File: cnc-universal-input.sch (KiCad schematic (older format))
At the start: 125 parts, among them J1 3PT, J10 2PT, J11 8PT, J12 USB_B_Mini, J13 2PT, J14 2PT, J2 3PT, J3 3PT, J4 3PT, J5 3PT, J6 3PT, J7 3PT, J8 3PT, J9 AVR-ISP-6, Q1 2N7002, Q11 2N7002, Q12 2N7002, Q13 2N7002, SW1 RESET, SW2 BTN, U1 ATmega328PB, U10 SFH617A-4, U11 SFH617A-4, U12 SFH617A-4, U13 SFH617A-4, U14 SFH617A-4, U15 SFH617A-4, U16 SFH617A-4, U18 CH340G, U19 TS2596S, U2 74HC595, U3 74HC595, U4 74HC595, U5 4051, U6 TS2596S, U8 LM7321, U9 SFH617A-4, Y1 18.432Mhz, Y2 12MHz

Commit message: Couldn't find a single 328PB non AU
Atmega328PB-AU is the only 328 I could get...
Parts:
- removed R1: 330, Resistor_SMD:R_0805_2012Metric, symbol Device:R_Small
- removed U1: ATmega328PB, Package_QFP:TQFP-32_7x7mm_P0.8mm, symbol MCU_Microchip_ATmega:ATmega328P-AU
- added U1: ATmega328PB-AU, Package_QFP:TQFP-32_7x7mm_P0.8mm, symbol MCU_Microchip_ATmega:ATmega328PB-AU
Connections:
- no-connect marks 12 -> 14
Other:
- moved on the sheet: C9
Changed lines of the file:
@@
 	0    1    1    0
 $EndComp
-$Comp
-L MCU_Microchip_ATmega:ATmega328P-AU U1
-U 1 1 5FED5CD7
-P 10550 6200
-F 0 "U1" H 10900 7700 50  0000 C CNN
-F 1 "ATmega328PB" V 10500 6300 50  0000 C CNN
-F 2 "Package_QFP:TQFP-32_7x7mm_P0.8mm" H 10550 6200 50  0001 C CIN
-F 3 "http://ww1.microchip.com/downloads/en/DeviceDoc/ATmega328_P%20AVR%20MCU%20with%20picoPower%20Technology%20Data%20Sheet%2040001984A.pdf" H 10550 6200 50  0001 C CNN
-	1    10550 6200
-	1    0    0    -1
-$EndComp
 Wire Wire Line
 	13550 1300 13550 1650
@@
 $EndComp
 Connection ~ 7150 3450
-Text Label 9850 5200 2    50   ~ 0
+Text Label 9850 6900 2    50   ~ 0
 ASIN
 Wire Wire Line
-	9850 5200 9900 5200
+	9850 6900 9900 6900
 Text Label 7350 3450 0    50   ~ 0
 OA
@@
 L Device:C_Small C9
 U 1 1 61DDCFEB
-P 9500 5150
-F 0 "C9" V 9350 5200 50  0000 L CNN
-F 1 "100nF" V 9350 5000 50  0000 L CNN
-F 2 "Capacitor_SMD:C_0805_2012Metric" H 9500 5150 50  0001 C CNN
-F 3 "~" H 9500 5150 50  0001 C CNN
-	1    9500 5150
+P 9800 5150
+F 0 "C9" V 9650 5300 50  0000 L CNN
+F 1 "100nF" V 9650 5000 50  0000 L CNN
+F 2 "Capacitor_SMD:C_0805_2012Metric" H 9800 5150 50  0001 C CNN
+F 3 "~" H 9800 5150 50  0001 C CNN
+	1    9800 5150
 	1    0    0    -1
 $EndComp
 Wire Wire Line
-	9500 5050 9500 5000
+	9800 5050 9800 5000
 Wire Wire Line
-	9500 5000 9950 5000
+	9800 5000 9950 5000
 Wire Wire Line
-	9500 5250 9500 5600
+	9800 5250 9800 5300
 $Comp
 L power:GND #PWR0185
 U 1 1 61E7EF53
-P 9500 5600
-F 0 "#PWR0185" H 9500 5350 50  0001 C CNN
-F 1 "GND" H 9505 5427 50  0000 C CNN
-F 2 "" H 9500 5600 50  0001 C CNN
-F 3 "" H 9500 5600 50  0001 C CNN
-	1    9500 5600
+P 9800 5300
+F 0 "#PWR0185" H 9800 5050 50  0001 C CNN
+F 1 "GND" H 9805 5127 50  0000 C CNN
+F 2 "" H 9800 5300 50  0001 C CNN
+F 3 "" H 9800 5300 50  0001 C CNN
+	1    9800 5300
 	1    0    0    -1
 $EndComp
@@
 	1    0    0    -1
 $EndComp
-$Comp
-L Device:R_Small R1
-U 1 1 688EAC57
-P 11250 8400
-F 0 "R1" V 11150 8350 50  0000 L CNN
-F 1 "330" V 11350 8350 50  0000 L CNN
-F 2 "Resistor_SMD:R_0805_2012Metric" H 11250 8400 50  0001 C CNN
-F 3 "~" H 11250 8400 50  0001 C CNN
-	1    11250 8400
-	1    0    0    -1
-$EndComp
 Wire Wire Line
-	11250 8500 11250 8550
+	11250 8300 11250 8550
 Wire Wire Line
 	11250 8550 11400 8550
@@
 $EndComp
 Wire Wire Line
-	9950 5300 9900 5300
+	9950 7000 9900 7000
 Wire Wire Line
-	9900 5300 9900 5200
-Connection ~ 9900 5200
+	9900 7000 9900 6900
+Connection ~ 9900 6900
 Wire Wire Line
-	9900 5200 9950 5200
+	9900 6900 9950 6900
+$Comp
+L MCU_Microchip_ATmega:ATmega328PB-AU U1
+U 1 1 609CE2BE
+P 10550 6200
+F 0 "U1" H 10550 4611 50  0000 C CNN
+F 1 "ATmega328PB-AU" H 10550 4520 50  0000 C CNN
+F 2 "Package_QFP:TQFP-32_7x7mm_P0.8mm" H 10550 6200 50  0001 C CIN
+F 3 "http://ww1.microchip.com/downloads/en/DeviceDoc/40001906C.pdf" H 10550 6200 50  0001 C CNN
+	1    10550 6200
+	1    0    0    -1
+$EndComp
+NoConn ~ 9950 6700
+NoConn ~ 9950 6800
 $EndSCHEMATC

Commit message: Changed Footprint
5mm rm buzzers don't exist
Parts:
- BZ1: footprint Buzzer_Beeper:Buzzer_TDK_PS1240P02BT_D12.2mm_H6.5mm -> Buzzer_Beeper:MagneticBuzzer_ProSignal_ABT-410-RC
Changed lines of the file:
@@
 F 0 "BZ1" H 11652 8679 50  0000 L CNN
 F 1 "Buzzer" H 11652 8588 50  0000 L CNN
-F 2 "Buzzer_Beeper:Buzzer_TDK_PS1240P02BT_D12.2mm_H6.5mm" V 11475 8750 50  0001 C CNN
+F 2 "Buzzer_Beeper:MagneticBuzzer_ProSignal_ABT-410-RC" V 11475 8750 50  0001 C CNN
 F 3 "~" V 11475 8750 50  0001 C CNN
 	1    11500 8650

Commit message: Yeetus deletus
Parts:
- removed R64: 1K, Resistor_SMD:R_0805_2012Metric, symbol Device:R_Small
- removed R65: 10K, Resistor_SMD:R_0805_2012Metric, symbol Device:R_Small
- removed Y1: 18.432Mhz, Crystal:Crystal_HC49-4H_Vertical, symbol Device:Crystal_Small
- added C29: 100nF, Capacitor_SMD:C_0805_2012Metric, symbol Device:C_Small
- added Y1: 18.432MHz, Crystal:Crystal_SMD_EuroQuartz_MJ-4Pin_5.0x3.2mm, symbol Device:Crystal_GND24
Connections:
- net +5V: now also C29.1
- net GND: now also C1.2, C29.2, Y1.2, Y1.4; no longer C1.1
- net at U1.7 (XTAL1/PB6): now also C2.2, Y1.1; no longer C1.2
- net at U1.8 (XTAL2/PB7): now also C1.1, Y1.3; no longer C2.2
- net at U1.28 (PC5): now also SW2.2
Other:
- moved on the sheet: C1, C2
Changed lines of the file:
@@
 SCK
 Wire Wire Line
-	11150 5600 11700 5600
-Wire Wire Line
-	11700 5600 11700 5500
-Wire Wire Line
-	11150 5700 11700 5700
-Wire Wire Line
-	11700 5700 11700 5800
+	11150 5600 11750 5600
 Wire Wire Line
 	11150 5000 11300 5000
@@
 	11150 7300 11300 7300
 $Comp
-L Device:Crystal_Small Y1
-U 1 1 5FFCDF62
-P 11800 5650
-F 0 "Y1" V 11754 5738 50  0000 L CNN
-F 1 "18.432Mhz" H 11600 6100 50  0000 L CNN
-F 2 "Crystal:Crystal_HC49-4H_Vertical" H 11800 5650 50  0001 C CNN
-F 3 "~" H 11800 5650 50  0001 C CNN
-	1    11800 5650
-	0    1    1    0
-$EndComp
-Wire Wire Line
-	11800 5550 11800 5500
-Wire Wire Line
-	11800 5500 11700 5500
-Wire Wire Line
-	11800 5750 11800 5800
-Wire Wire Line
-	11800 5800 11700 5800
-Wire Wire Line
-	11800 5500 11850 5500
-Connection ~ 11800 5500
-Wire Wire Line
-	11800 5800 11850 5800
-Connection ~ 11800 5800
-$Comp
 L Device:C_Small C1
 U 1 1 5FFE32BF
-P 11950 5500
-F 0 "C1" V 11800 5550 50  0000 L CNN
-F 1 "30pF" V 11800 5350 50  0000 L CNN
-F 2 "Capacitor_SMD:C_0805_2012Metric" H 11950 5500 50  0001 C CNN
-F 3 "~" H 11950 5500 50  0001 C CNN
-	1    11950 5500
+P 12050 5250
+F 0 "C1" V 11900 5300 50  0000 L CNN
+F 1 "30pF" H 12000 5450 50  0000 L CNN
+F 2 "Capacitor_SMD:C_0805_2012Metric" H 12050 5250 50  0001 C CNN
+F 3 "~" H 12050 5250 50  0001 C CNN
+	1    12050 5250
 	0    1    1    0
 $EndComp
@@
 L Device:C_Small C2
 U 1 1 5FFE4081
-P 11950 5800
-F 0 "C2" V 12050 5850 50  0000 L CNN
-F 1 "30pF" V 12050 5650 50  0000 L CNN
-F 2 "Capacitor_SMD:C_0805_2012Metric" H 11950 5800 50  0001 C CNN
-F 3 "~" H 11950 5800 50  0001 C CNN
-	1    11950 5800
+P 11850 5250
+F 0 "C2" V 11950 5300 50  0000 L CNN
+F 1 "30pF" H 11800 5050 50  0000 L CNN
+F 2 "Capacitor_SMD:C_0805_2012Metric" H 11850 5250 50  0001 C CNN
+F 3 "~" H 11850 5250 50  0001 C CNN
+	1    11850 5250
 	0    1    1    0
 $EndComp
-Wire Wire Line
-	12050 5500 12150 5500
-Wire Wire Line
-	12150 5500 12150 5800
-Wire Wire Line
-	12150 5800 12050 5800
-Wire Wire Line
-	12150 5800 12150 5900
-Connection ~ 12150 5800
 $Comp
 L power:GND #PWR0118
 U 1 1 5FFEFB10
-P 12150 5900
-F 0 "#PWR0118" H 12150 5650 50  0001 C CNN
-F 1 "GND" H 12155 5727 50  0000 C CNN
-F 2 "" H 12150 5900 50  0001 C CNN
-F 3 "" H 12150 5900 50  0001 C CNN
-	1    12150 5900
+P 11950 5400
+F 0 "#PWR0118" H 11950 5150 50  0001 C CNN
+F 1 "GND" H 11955 5227 50  0000 C CNN
+F 2 "" H 11950 5400 50  0001 C CNN
+F 3 "" H 11950 5400 50  0001 C CNN
+	1    11950 5400
 	1    0    0    -1
 $EndComp
@@
 $EndComp
 $Comp
-L Device:R_Small R64
-U 1 1 6197C82D
-P 12050 6400
-F 0 "R64" V 11950 6400 50  0000 L CNN
-F 1 "1K" V 12150 6350 50  0000 L CNN
-F 2 "Resistor_SMD:R_0805_2012Metric" H 12050 6400 50  0001 C CNN
-F 3 "~" H 12050 6400 50  0001 C CNN
-	1    12050 6400
-	0    1    1    0
-$EndComp
-Wire Wire Line
-	11150 6400 11950 6400
-Wire Wire Line
-	12150 6400 12400 6400
-$Comp
-L Device:R_Small R65
-U 1 1 61A1B151
-P 12400 6200
-F 0 "R65" V 12300 6200 50  0000 L CNN
-F 1 "10K" V 12500 6150 50  0000 L CNN
-F 2 "Resistor_SMD:R_0805_2012Metric" H 12400 6200 50  0001 C CNN
-F 3 "~" H 12400 6200 50  0001 C CNN
-	1    12400 6200
-	-1   0    0    1
-$EndComp
-$Comp
-L power:+5V #PWR0183
-U 1 1 61B536B1
-P 12400 6050
-F 0 "#PWR0183" H 12400 5900 50  0001 C CNN
-F 1 "+5V" H 12415 6223 50  0000 C CNN
-F 2 "" H 12400 6050 50  0001 C CNN
-F 3 "" H 12400 6050 50  0001 C CNN
-	1    12400 6050
-	1    0    0    -1
-$EndComp
-Wire Wire Line
-	12400 6050 12400 6100
-$Comp
 L power:GND #PWR0184
 U 1 1 61BA31AD
@@
 Text Label 11300 6500 0    50   ~ 0
 ~RST
-Wire Wire Line
-	12400 6300 12400 6400
-Connection ~ 12400 6400
 $Comp
 L Device:C_Small C9
@@
 NoConn ~ 9950 6700
 NoConn ~ 9950 6800
+Wire Wire Line
+	11150 6400 12400 6400
+$Comp
+L Device:C_Small C29
+U 1 1 60BC2628
+P 11900 7700
+F 0 "C29" H 11992 7746 50  0000 L CNN
+F 1 "100nF" V 11750 7500 50  0000 L CNN
+F 2 "Capacitor_SMD:C_0805_2012Metric" H 11900 7700 50  0001 C CNN
+F 3 "~" H 11900 7700 50  0001 C CNN
+	1    11900 7700
+	1    0    0    -1
+$EndComp
+$Comp
+L power:+5V #PWR0166
+U 1 1 60BC262E
+P 11900 7600
+F 0 "#PWR0166" H 11900 7450 50  0001 C CNN
+F 1 "+5V" H 11915 7773 50  0000 C CNN
+F 2 "" H 11900 7600 50  0001 C CNN
+F 3 "" H 11900 7600 50  0001 C CNN
+	1    11900 7600
+	1    0    0    -1
+$EndComp
+$Comp
+L power:GND #PWR0167
+U 1 1 60BC2634
+P 11900 7800
+F 0 "#PWR0167" H 11900 7550 50  0001 C CNN
+F 1 "GND" H 11900 7650 50  0000 C CNN
+F 2 "" H 11900 7800 50  0001 C CNN
+F 3 "" H 11900 7800 50  0001 C CNN
+	1    11900 7800
+	1    0    0    -1
+$EndComp
+$Comp
+L Device:Crystal_GND24 Y1
+U 1 1 60C7D282
+P 11950 4950
+F 0 "Y1" H 12144 4996 50  0000 L CNN
+F 1 "18.432MHz" V 11650 4800 50  0000 L CNN
+F 2 "Crystal:Crystal_SMD_EuroQuartz_MJ-4Pin_5.0x3.2mm" H 11950 4950 50  0001 C CNN
+F 3 "~" H 11950 4950 50  0001 C CNN
+	1    11950 4950
+	1    0    0    -1
+$EndComp
+Wire Wire Line
+	11800 4950 11750 4950
+Wire Wire Line
+	11750 4950 11750 5250
+Wire Wire Line
+	12150 5700 12150 5250
+Wire Wire Line
+	12150 4950 12100 4950
+Wire Wire Line
+	11150 5700 12150 5700
+Wire Wire Line
+	11950 5150 11950 5250
+Connection ~ 11950 5250
+Wire Wire Line
+	11950 5250 11950 5400
+Connection ~ 11750 5250
+Wire Wire Line
+	11750 5250 11750 5600
+Connection ~ 12150 5250
+Wire Wire Line
+	12150 5250 12150 4950
+$Comp
+L power:GND #PWR0169
+U 1 1 60EB164C
+P 12150 4600
+F 0 "#PWR0169" H 12150 4350 50  0001 C CNN
+F 1 "GND" H 12155 4427 50  0000 C CNN
+F 2 "" H 12150 4600 50  0001 C CNN
+F 3 "" H 12150 4600 50  0001 C CNN
+	1    12150 4600
+	1    0    0    -1
+$EndComp
+Wire Wire Line
+	12150 4600 12150 4550
+Wire Wire Line
+	12150 4550 11950 4550
+Wire Wire Line
+	11950 4550 11950 4750
 $EndSCHEMATC

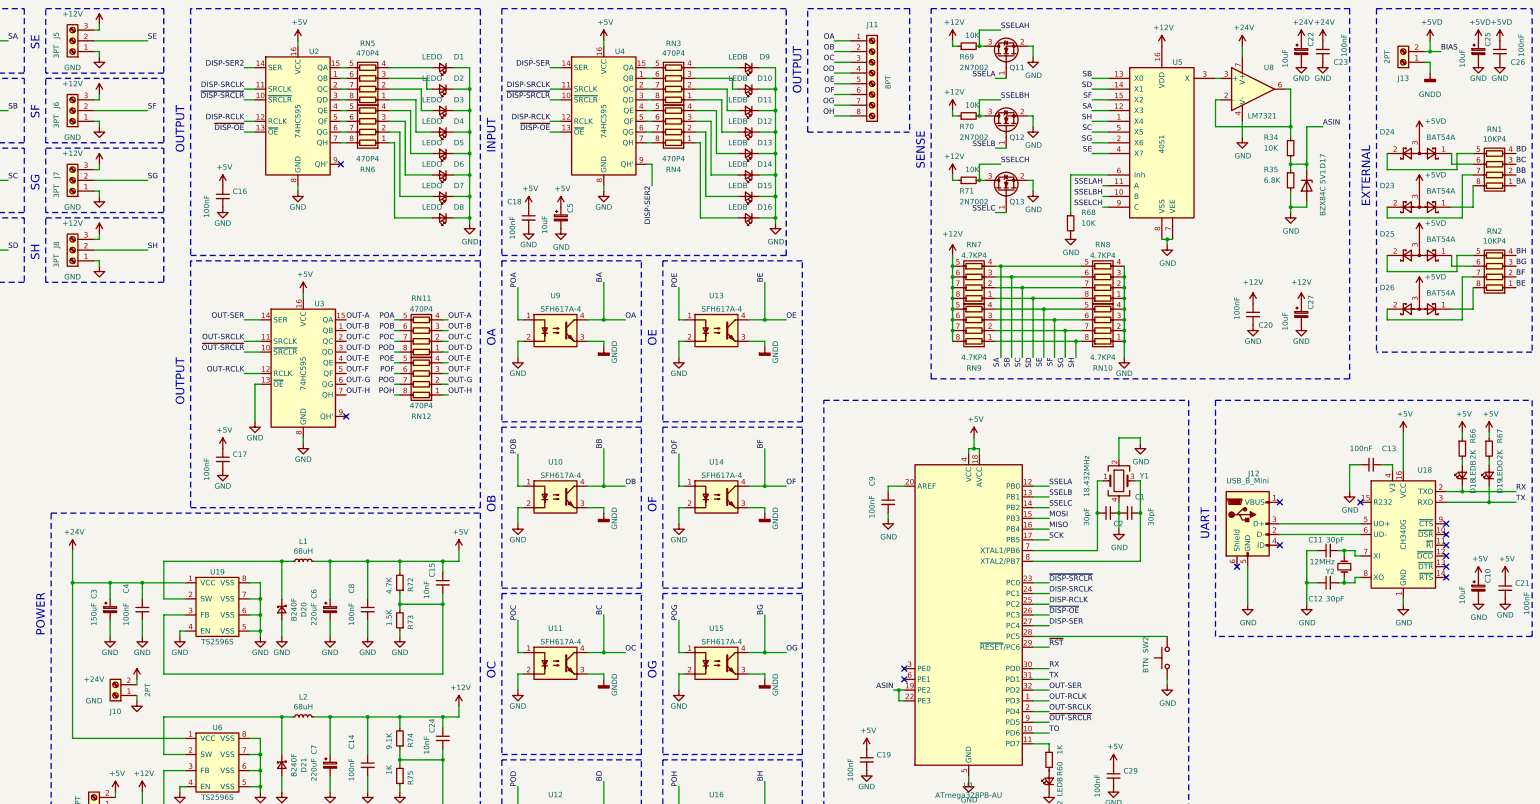
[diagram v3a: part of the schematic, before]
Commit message: Board stuff
Flipped the input polarity
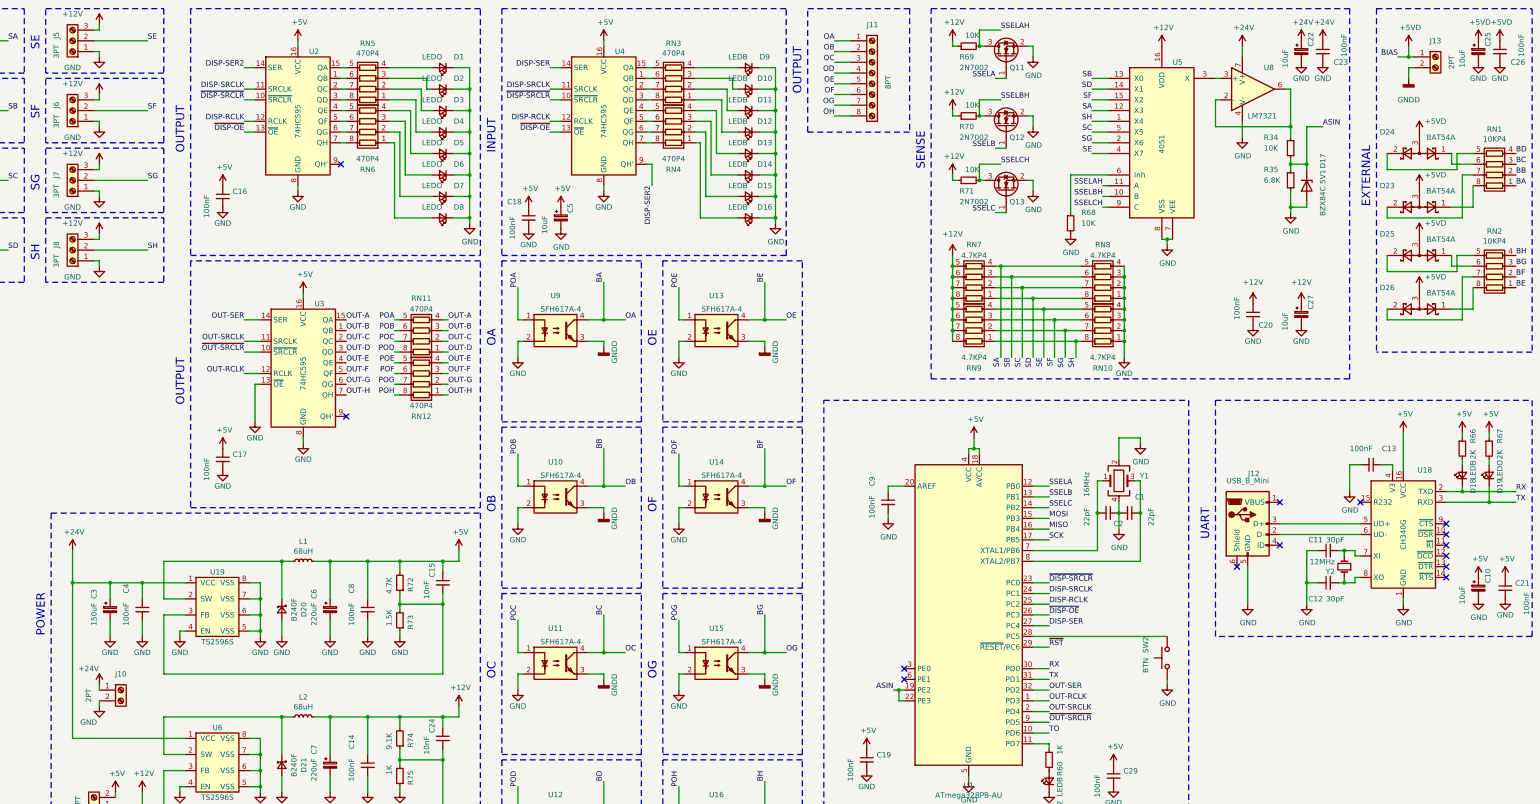
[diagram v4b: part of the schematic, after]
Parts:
- C1, C2: value 30pF -> 22pF
- Y1: value 18.432MHz -> 16MHz
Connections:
- net +24V: now also J10.1 (Pin_1); no longer J10.2 (Pin_2)
- net +5VD: now also J13.1 (Pin_1); no longer J13.2 (Pin_2)
- net GND: now also J10.2 (Pin_2); no longer J10.1 (Pin_1)
- net GNDD: now also J13.2 (Pin_2); no longer J13.1 (Pin_1)
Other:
- moved on the sheet: J10, J13
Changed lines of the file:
@@
 P 12050 5250
 F 0 "C1" V 11900 5300 50  0000 L CNN
-F 1 "30pF" H 12000 5450 50  0000 L CNN
+F 1 "22pF" H 12000 5450 50  0000 L CNN
 F 2 "Capacitor_SMD:C_0805_2012Metric" H 12050 5250 50  0001 C CNN
 F 3 "~" H 12050 5250 50  0001 C CNN
@@
 P 11850 5250
 F 0 "C2" V 11950 5300 50  0000 L CNN
-F 1 "30pF" H 11800 5050 50  0000 L CNN
+F 1 "22pF" H 11800 5050 50  0000 L CNN
 F 2 "Capacitor_SMD:C_0805_2012Metric" H 11850 5250 50  0001 C CNN
 F 3 "~" H 11850 5250 50  0001 C CNN
@@
 	6750 1700 6650 1700
 $Comp
-L Connector:Screw_Terminal_01x02 J10
-U 1 1 603C6C3F
-P 2600 6950
-F 0 "J10" H 2600 7100 50  0000 C CNN
-F 1 "2PT" V 2300 6900 50  0000 C CNN
-F 2 "TerminalBlock_RND:TerminalBlock_RND_205-00001_1x02_P5.00mm_Horizontal" H 2600 6950 50  0001 C CNN
-F 3 "~" H 2600 6950 50  0001 C CNN
-	1    2600 6950
-	-1   0    0    1
-$EndComp
-$Comp
-L power:+24V #PWR0132
-U 1 1 60454363
-P 2800 6800
-F 0 "#PWR0132" H 2800 6650 50  0001 C CNN
-F 1 "+24V" H 2400 6800 50  0000 C CNN
-F 2 "" H 2800 6800 50  0001 C CNN
-F 3 "" H 2800 6800 50  0001 C CNN
-	1    2800 6800
-	1    0    0    -1
-$EndComp
-$Comp
-L power:GND #PWR0133
-U 1 1 60454751
-P 2800 7000
-F 0 "#PWR0133" H 2800 6750 50  0001 C CNN
-F 1 "GND" H 2400 7000 50  0000 C CNN
-F 2 "" H 2800 7000 50  0001 C CNN
-F 3 "" H 2800 7000 50  0001 C CNN
-	1    2800 7000
-	1    0    0    -1
-$EndComp
-Wire Wire Line
-	2800 6800 2800 6850
-Wire Wire Line
-	2800 6950 2800 7000
-$Comp
 L power:+5V #PWR0134
 U 1 1 60507A16
@@
 	4150 7500 4150 7150
 Wire Wire Line
-	4150 7150 3050 7150
-Wire Wire Line
-	3050 7150 3050 7500
-Wire Wire Line
-	3050 7500 3250 7500
-Wire Wire Line
 	4150 7150 4250 7150
 Connection ~ 4150 7150
@@
 Wire Wire Line
 	5650 7550 5650 8200
-Wire Wire Line
-	5650 8200 3050 8200
-Wire Wire Line
-	3050 8200 3050 7650
-Wire Wire Line
-	3050 7650 3250 7650
 Connection ~ 5250 7550
 Wire Wire Line
@@
 Wire Wire Line
 	2600 7850 2600 7900
-$Comp
-L power:+12V #PWR0225
-U 1 1 631F5904
-P 2850 7850
-F 0 "#PWR0225" H 2850 7700 50  0001 C CNN
-F 1 "+12V" H 2865 8023 50  0000 C CNN
-F 2 "" H 2850 7850 50  0001 C CNN
-F 3 "" H 2850 7850 50  0001 C CNN
-	1    2850 7850
-	1    0    0    -1
-$EndComp
-$Comp
-L power:+5V #PWR0226
-U 1 1 631F61BE
-P 2600 7850
-F 0 "#PWR0226" H 2600 7700 50  0001 C CNN
-F 1 "+5V" H 2615 8023 50  0000 C CNN
-F 2 "" H 2600 7850 50  0001 C CNN
-F 3 "" H 2600 7850 50  0001 C CNN
-	1    2600 7850
-	1    0    0    -1
-$EndComp
 Wire Wire Line
 	2600 8000 2850 8000
@@
 	1    0    0    -1
 $EndComp
-Connection ~ 14850 950
 Wire Wire Line
-	14850 950  14950 950
+	14650 1000 14550 1000
 $Comp
 L power:GNDD #PWR0189
 U 1 1 5FFA09F8
-P 14850 1150
-F 0 "#PWR0189" H 14850 900 50  0001 C CNN
-F 1 "GNDD" H 14850 950 50  0000 C CNN
-F 2 "" H 14850 1150 50  0001 C CNN
-F 3 "" H 14850 1150 50  0001 C CNN
-	1    14850 1150
+P 14650 1200
+F 0 "#PWR0189" H 14650 950 50  0001 C CNN
+F 1 "GNDD" H 14650 1000 50  0000 C CNN
+F 2 "" H 14650 1200 50  0001 C CNN
+F 3 "" H 14650 1200 50  0001 C CNN
+	1    14650 1200
 	1    0    0    -1
 $EndComp
 Wire Wire Line
-	14850 1050 14850 1150
+	14650 1000 14650 900
 Wire Wire Line
-	14800 1050 14850 1050
+	14700 1000 14650 1000
 Wire Wire Line
-	14850 950  14800 950
+	14650 1100 14700 1100
 Wire Wire Line
-	14850 850  14850 950
+	14650 1200 14650 1100
 $Comp
 L power:+5VD #PWR0188
 U 1 1 5FEF3703
-P 14850 850
-F 0 "#PWR0188" H 14850 700 50  0001 C CNN
-F 1 "+5VD" H 14865 1023 50  0000 C CNN
-F 2 "" H 14850 850 50  0001 C CNN
-F 3 "" H 14850 850 50  0001 C CNN
-	1    14850 850
+P 14650 900
+F 0 "#PWR0188" H 14650 750 50  0001 C CNN
+F 1 "+5VD" H 14665 1073 50  0000 C CNN
+F 2 "" H 14650 900 50  0001 C CNN
+F 3 "" H 14650 900 50  0001 C CNN
+	1    14650 900
 	1    0    0    -1
 $EndComp
@@
 L Connector:Screw_Terminal_01x02 J13
 U 1 1 5FEF2B76
-P 14600 1050
-F 0 "J13" H 14600 1200 50  0000 C CNN
-F 1 "2PT" V 14750 1000 50  0000 C CNN
-F 2 "TerminalBlock_RND:TerminalBlock_RND_205-00001_1x02_P5.00mm_Horizontal" H 14600 1050 50  0001 C CNN
-F 3 "~" H 14600 1050 50  0001 C CNN
-	1    14600 1050
-	-1   0    0    1
+P 14900 1000
+F 0 "J13" H 14900 1150 50  0000 C CNN
+F 1 "2PT" V 15050 950 50  0000 C CNN
+F 2 "TerminalBlock_RND:TerminalBlock_RND_205-00001_1x02_P5.00mm_Horizontal" H 14900 1000 50  0001 C CNN
+F 3 "~" H 14900 1000 50  0001 C CNN
+	1    14900 1000
+	1    0    0    -1
 $EndComp
-Text Label 14950 950  0    50   ~ 0
+Text Label 14550 1000 2    50   ~ 0
 BIAS
 Text Label 8650 6200 1    50   ~ 0
@@
 	1    0    0    -1
 $EndComp
-$Comp
-L Device:Crystal_GND24 Y1
-U 1 1 60C7D282
-P 11950 4950
-F 0 "Y1" H 12144 4996 50  0000 L CNN
-F 1 "18.432MHz" V 11650 4800 50  0000 L CNN
-F 2 "Crystal:Crystal_SMD_EuroQuartz_MJ-4Pin_5.0x3.2mm" H 11950 4950 50  0001 C CNN
-F 3 "~" H 11950 4950 50  0001 C CNN
-	1    11950 4950
-	1    0    0    -1
-$EndComp
 Wire Wire Line
 	11800 4950 11750 4950
@@
 Wire Wire Line
 	11950 4550 11950 4750
+Wire Wire Line
+	3050 7650 3250 7650
+Wire Wire Line
+	5650 8200 3050 8200
+Wire Wire Line
+	3050 8200 3050 7650
+Wire Wire Line
+	3050 7500 3250 7500
+Wire Wire Line
+	4150 7150 3050 7150
+Wire Wire Line
+	3050 7150 3050 7500
+Wire Wire Line
+	2450 6900 2450 6850
+Wire Wire Line
+	2450 7050 2450 7000
+$Comp
+L power:GND #PWR0133
+U 1 1 60454751
+P 2450 7050
+F 0 "#PWR0133" H 2450 6800 50  0001 C CNN
+F 1 "GND" H 2350 6900 50  0000 C CNN
+F 2 "" H 2450 7050 50  0001 C CNN
+F 3 "" H 2450 7050 50  0001 C CNN
+	1    2450 7050
+	1    0    0    -1
+$EndComp
+$Comp
+L Connector:Screw_Terminal_01x02 J10
+U 1 1 603C6C3F
+P 2650 6900
+F 0 "J10" H 2650 7050 50  0000 C CNN
+F 1 "2PT" V 2350 6850 50  0000 C CNN
+F 2 "TerminalBlock_RND:TerminalBlock_RND_205-00001_1x02_P5.00mm_Horizontal" H 2650 6900 50  0001 C CNN
+F 3 "~" H 2650 6900 50  0001 C CNN
+	1    2650 6900
+	1    0    0    -1
+$EndComp
+$Comp
+L power:+24V #PWR0132
+U 1 1 60454363
+P 2450 6850
+F 0 "#PWR0132" H 2450 6700 50  0001 C CNN
+F 1 "+24V" H 2350 7000 50  0000 C CNN
+F 2 "" H 2450 6850 50  0001 C CNN
+F 3 "" H 2450 6850 50  0001 C CNN
+	1    2450 6850
+	1    0    0    -1
+$EndComp
+$Comp
+L Device:Crystal_GND24 Y1
+U 1 1 60C7D282
+P 11950 4950
+F 0 "Y1" H 12144 4996 50  0000 L CNN
+F 1 "16MHz" V 11650 4800 50  0000 L CNN
+F 2 "Crystal:Crystal_SMD_EuroQuartz_MJ-4Pin_5.0x3.2mm" H 11950 4950 50  0001 C CNN
+F 3 "~" H 11950 4950 50  0001 C CNN
+	1    11950 4950
+	1    0    0    -1
+$EndComp
+$Comp
+L power:+5V #PWR0226
+U 1 1 631F61BE
+P 2600 7850
+F 0 "#PWR0226" H 2600 7700 50  0001 C CNN
+F 1 "+5V" H 2615 8023 50  0000 C CNN
+F 2 "" H 2600 7850 50  0001 C CNN
+F 3 "" H 2600 7850 50  0001 C CNN
+	1    2600 7850
+	1    0    0    -1
+$EndComp
+$Comp
+L power:+12V #PWR0225
+U 1 1 631F5904
+P 2850 7850
+F 0 "#PWR0225" H 2850 7700 50  0001 C CNN
+F 1 "+12V" H 2865 8023 50  0000 C CNN
+F 2 "" H 2850 7850 50  0001 C CNN
+F 3 "" H 2850 7850 50  0001 C CNN
+	1    2850 7850
+	1    0    0    -1
+$EndComp
+Connection ~ 14650 1000
 $EndSCHEMATC
